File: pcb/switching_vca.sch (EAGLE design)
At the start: 11 parts, among them Q1 MOSFET-PCHANNELSMD, Q2 SST5484, U1 LM319

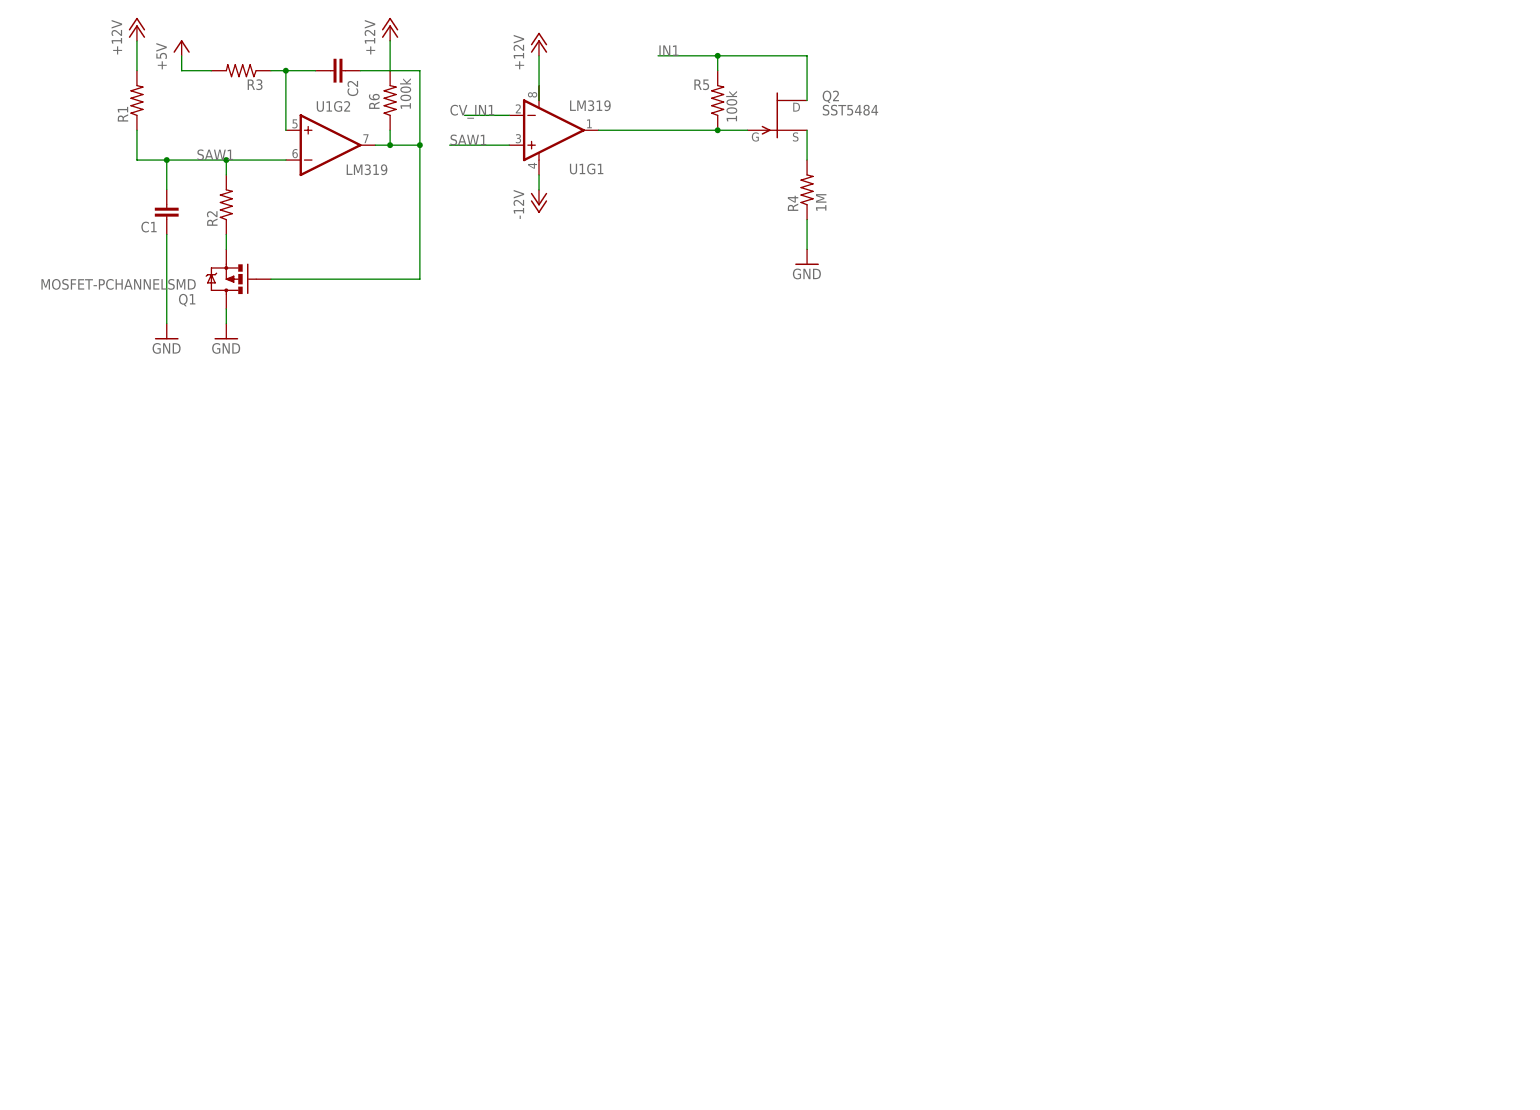
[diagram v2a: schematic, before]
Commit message: First attempt at schem (footprints not specced), initial BOM
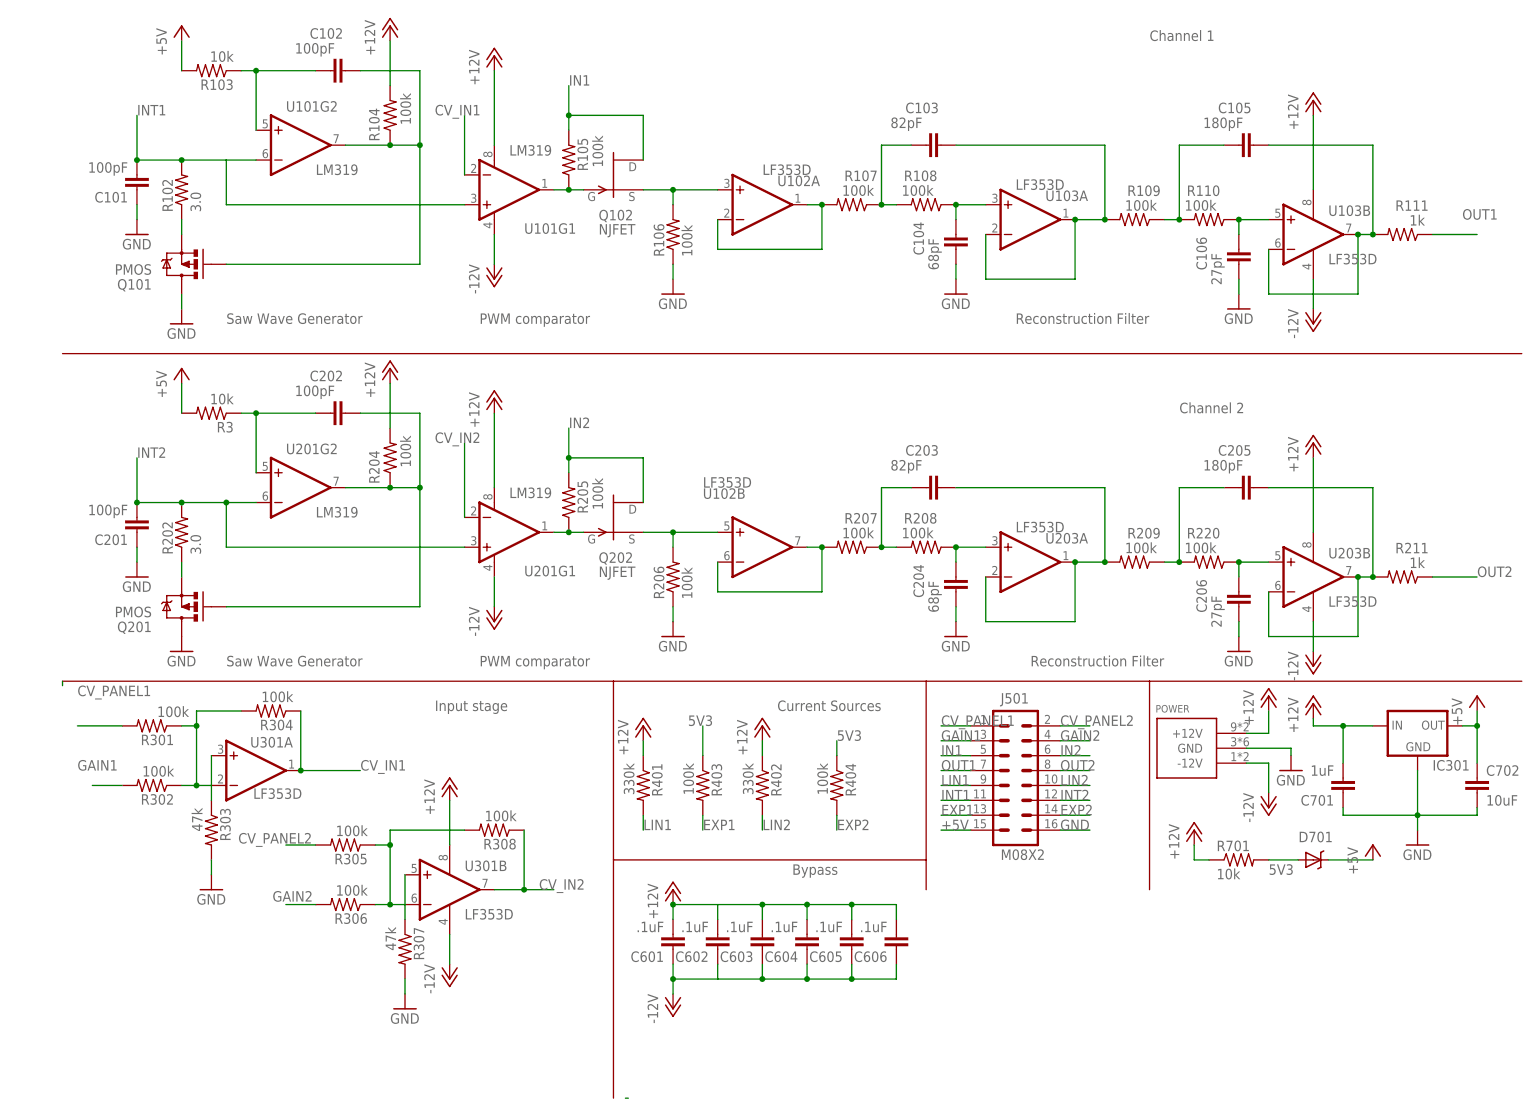
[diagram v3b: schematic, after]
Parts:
- removed C1: (no value), SparkFun:CAP1210
- removed Q1: MOSFET-PCHANNELSMD, SparkFun:MOSFET-PCHANNELSMD
- removed Q2: SST5484, transistor-fet:SST5484
- removed R1, R2: (no value), SparkFun:RESISTOR0603-RES
- removed R4: 1M, SparkFun:RESISTOR0603-RES
- removed R5, R6: 100k, SparkFun:RESISTOR0603-RES
- removed U1: LM319, SparkFun:LM393
- added C101, C201, C202: 100pF, SparkFun:CAP1210
- added C103, C203: 82pF, SparkFun:CAP1210
- added C104, C204: 68pF, SparkFun:CAP1210
- added C105, C205: 180pF, SparkFun:CAP1210
- added C106, C206: 27pF, SparkFun:CAP1210
- added C601, C602, C603, C604, C605, C606: .1uF, SparkFun:CAP1210
- added C701: 1uF, SparkFun:CAP0805
- added C702: 10uF, SparkFun:CAP1206
- added D701: DIODE-SCHOTTKY, SparkFun:DIODE-SCHOTTKY
- added IC301: V_REG_MIC2920, SparkFun:V_REG_MIC2920
- added J501: M08X2, SparkFun:M08X2
- added POWER: POWER_SIMPLE16, eurorack:POWER_SIMPLE16
- added Q101, Q201: PMOS, SparkFun:MOSFET-PCHANNELSMD
- added Q102, Q202: NJFET, transistor-fet:SST5484
- added R102, R202: 3.0, SparkFun:RESISTOR0603-RES
- added R103, R701: 10k, SparkFun:RESISTOR0603-RES
- added R104, R105, R106, R107, R108, R109, R110, R204, R205, R206, R207, R208, R209, R220, R301, R302, R304, R305, R306, R308, R403, R404: 100k, SparkFun:RESISTOR0603-RES
- added R111, R211: 1k, SparkFun:RESISTOR0603-RES
- added R303, R307: 47k, SparkFun:RESISTOR0603-RES
- added R401, R402: 330k, SparkFun:RESISTOR0603-RES
- added U101, U201: LM319, SparkFun:LM393
- added U102, U103, U203, U301: LF353D, linear:LF353D
- C102: value (none) -> 100pF
- R3: value (none) -> 10k
- renumbered C2 to C102
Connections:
- removed net SAW1: C1.2, R1.1, R2.2, U1G1.+IN, U1G2.-IN
- new net -12V: C601.1, C602.1, C603.1, C604.1, C605.1, C606.1, POWER.-12V, U101G1.V-, U103P.V-, U201G1.V-, U203P.V-, U301P.V-
- new net 5V3: D701.A, R403.1, R404.1, R701.2
- new net CV_IN2: R308.1, U201G1.-IN, U301B.OUT
- new net CV_PANEL1: J501.1, R301.2
- new net CV_PANEL2: J501.2, R305.2
- new net EXP1: J501.13, R403.2
- new net EXP2: J501.14, R404.2
- new net GAIN1: J501.3, R302.2
- new net GAIN2: J501.4, R306.2
- new net IN2: J501.6, Q202.D, R205.2
- new net INT1: C101.2, J501.11, R102.2, U101G1.+IN, U101G2.-IN
- new net INT2: C201.2, J501.12, R202.2, U201G1.+IN, U201G2.-IN
- new net LIN1: J501.9, R401.2
- new net LIN2: J501.10, R402.2
- new net N$10: C202.1, Q201.G, R204.1, U201G2.OUT
- new net N$11: C105.2, R109.1, R110.2
- new net N$12: C106.1, R110.1, U103B.+IN
- new net N$13: C105.1, R111.2, U103B.-IN, U103B.OUT
- new net N$15: Q202.G, R205.1, U201G1.OUT
- new net N$16: Q202.S, R206.2, U102B.+IN
- new net N$17: R207.2, U102B.-IN, U102B.OUT
- new net N$18: C203.1, R209.2, U203A.-IN, U203A.OUT
- new net N$19: C203.2, R207.1, R208.2
- new net N$2: R107.2, U102A.-IN, U102A.OUT
- new net N$20: C204.1, R208.1, U203A.+IN
- new net N$21: C205.2, R209.1, R220.2
- new net N$22: C206.1, R220.1, U203B.+IN
- new net N$23: C205.1, R211.2, U203B.-IN, U203B.OUT
- new net N$24: R307.1, U301B.+IN
- new net N$25: R303.1, U301A.+IN
- new net N$32: R305.1, R306.1, R308.2
- new net N$5: C103.1, R109.2, U103A.-IN, U103A.OUT
- new net N$7: C103.2, R107.1, R108.2
- new net N$8: C104.1, R108.1, U103A.+IN
- new net OUT1: J501.7, R111.1
- new net OUT2: J501.8, R211.1
- new net R102: Q201.S, R202.1
- new net R203: C202.2, R3.1, U201G2.+IN
- new net R301: R301.1, R302.1, R304.2, U301A.-IN
- net +12V: now also C601.2, C602.2, C603.2, C604.2, C605.2, C606.2, C701.2, IC301.IN, POWER.+12V, R104.2, R204.2, R401.1, R402.1, R701.1, U101G1.V+, U103P.V+, U201G1.V+, U203P.V+, U301P.V+; no longer R1.2, R6.2
- net +5V: now also C702.1, D701.C, IC301.OUT, J501.15, R103.2
- net CV_IN1: now also R304.1, U101G1.-IN, U301A.OUT; no longer U1G1.-IN
- net GND: now also C101.1, C104.2, C106.2, C201.1, C204.2, C206.2, C701.1, C702.2, IC301.GND, J501.16, POWER.GND, Q101.D, Q201.D, R106.1, R206.1, R303.2, R307.2; no longer C1.1, Q1.D, R4.1
- net IN1: now also J501.5, Q102.D, R105.2; no longer Q2.D, R5.2
- net N$: now also Q101.G, R104.1, U101G2.OUT; no longer Q1.G, R6.1, U1G2.OUT
- net N$1: now also Q101.S, R102.1; no longer Q1.S, R2.1
- net N$3: now also Q102.G, R105.1, U101G1.OUT; no longer Q2.G, R5.1, U1G1.OUT
- net N$4: now also R103.1, U101G2.+IN; no longer R3.1, U1G2.+IN
- net N$6: now also Q102.S, R106.2, U102A.+IN; no longer Q2.S, R4.2
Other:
- note added: "Bypass"
- note added: "Channel 1"
- note added: "Channel 2"
- note added: "Current Sources"
- note added: "Input stage"
- note added: "PWM comparator"
- note added: "Reconstruction Filter"
- note added: "Saw Wave Generator"
- moved on the sheet: R3

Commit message: added shitty board, made mouser bom
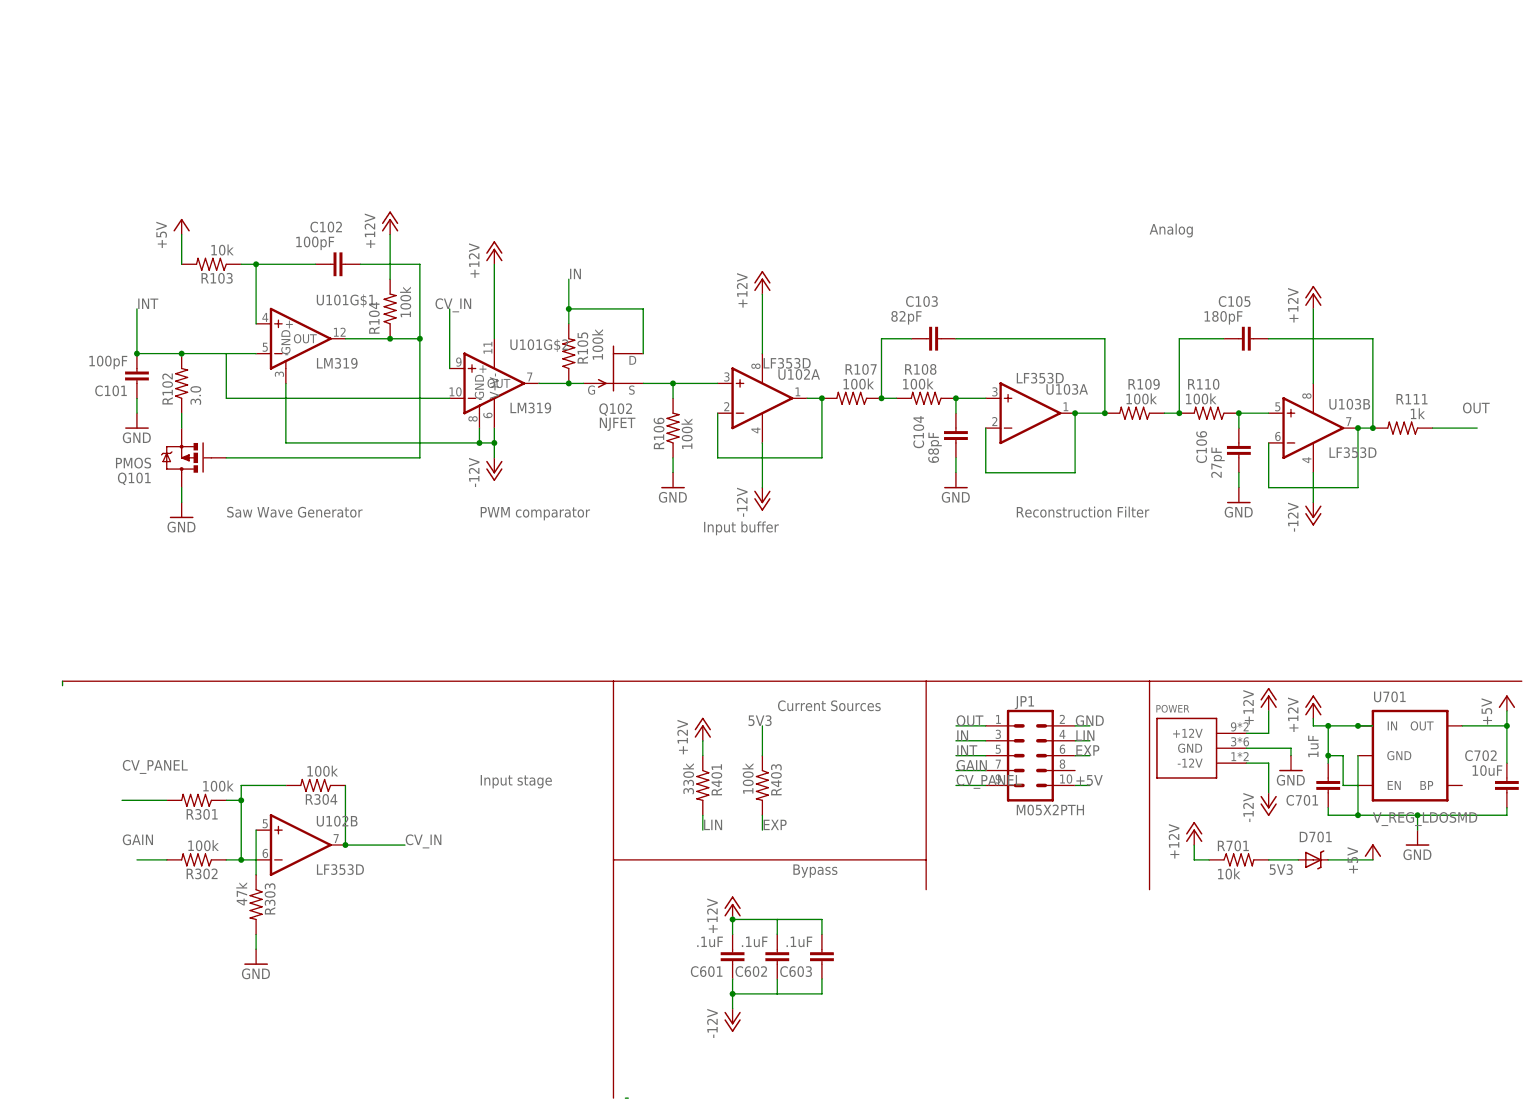
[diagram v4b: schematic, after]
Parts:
- removed C201, C202: 100pF, SparkFun:CAP1210
- removed C203: 82pF, SparkFun:CAP1210
- removed C204: 68pF, SparkFun:CAP1210
- removed C205: 180pF, SparkFun:CAP1210
- removed C206: 27pF, SparkFun:CAP1210
- removed C604, C605, C606: .1uF, SparkFun:CAP1210
- removed IC301: V_REG_MIC2920, SparkFun:V_REG_MIC2920
- removed J501: M08X2, SparkFun:M08X2
- removed Q201: PMOS, SparkFun:MOSFET-PCHANNELSMD
- removed Q202: NJFET, transistor-fet:SST5484
- removed R202: 3.0, SparkFun:RESISTOR0603-RES
- removed R204, R205, R206, R207, R208, R209, R220, R305, R306, R308, R404: 100k, SparkFun:RESISTOR0603-RES
- removed R211: 1k, SparkFun:RESISTOR0603-RES
- removed R3: 10k, SparkFun:RESISTOR0603-RES
- removed R307: 47k, SparkFun:RESISTOR0603-RES
- removed R402: 330k, SparkFun:RESISTOR0603-RES
- removed U201: LM319, SparkFun:LM393
- removed U203, U301: LF353D, linear:LF353D
- added JP1: M05X2PTH, SparkFun:M05X2PTH
- added U701: V_REG_LDOSMD, SparkFun:V_REG_LDOSMD
- C101, C102, C103, C104, C105, C106, C601, C602, C603: device SparkFun:CAP1210 -> SparkFun:CAP0603-CAP
- U101: device SparkFun:LM393 -> russruss:LM319
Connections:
- removed net CV_IN1: R304.1, U101G1.-IN, U301A.OUT
- removed net CV_IN2: R308.1, U201G1.-IN, U301B.OUT
- removed net CV_PANEL1: J501.1, R301.2
- removed net CV_PANEL2: J501.2, R305.2
- removed net EXP1: J501.13, R403.2
- removed net EXP2: J501.14, R404.2
- removed net GAIN1: J501.3, R302.2
- removed net GAIN2: J501.4, R306.2
- removed net IN1: J501.5, Q102.D, R105.2
- removed net IN2: J501.6, Q202.D, R205.2
- removed net INT1: C101.2, J501.11, R102.2, U101G1.+IN, U101G2.-IN
- removed net INT2: C201.2, J501.12, R202.2, U201G1.+IN, U201G2.-IN
- removed net LIN1: J501.9, R401.2
- removed net LIN2: J501.10, R402.2
- removed net N$15 (its old number): Q202.G, R205.1, U201G1.OUT
- removed net N$16: Q202.S, R206.2, U102B.+IN
- removed net N$17: R207.2, U102B.-IN, U102B.OUT
- removed net N$18: C203.1, R209.2, U203A.-IN, U203A.OUT
- removed net N$19: C203.2, R207.1, R208.2
- removed net N$20: C204.1, R208.1, U203A.+IN
- removed net N$21: C205.2, R209.1, R220.2
- removed net N$22: C206.1, R220.1, U203B.+IN
- removed net N$23: C205.1, R211.2, U203B.-IN, U203B.OUT
- removed net N$24: R307.1, U301B.+IN
- removed net N$25: R303.1, U301A.+IN
- removed net N$32: R305.1, R306.1, R308.2
- removed net OUT1: J501.7, R111.1
- removed net OUT2: J501.8, R211.1
- removed net R102: Q201.S, R202.1
- removed net R203: C202.2, R3.1, U201G2.+IN
- new net CV_IN: R304.1, U102B.OUT
- new net CV_PANEL: JP1.9, R301.2
- new net EXP: JP1.6, R403.2
- new net GAIN: JP1.7, R302.2
- new net IN: JP1.3, Q102.D, R105.2
- new net INT: C101.2, JP1.5, R102.2, U101G$1.-, U101G$2.-
- new net LIN: JP1.4, R401.2
- new net OUT: JP1.1, R111.1
- net +12V: now also U101G$3.V+, U102P.V+, U701.EN, U701.IN; no longer C604.2, C605.2, C606.2, IC301.IN, R204.2, R402.1, U101G1.V+, U201G1.V+, U203P.V+, U301P.V+
- net +5V: now also JP1.10, U701.OUT; no longer IC301.OUT, J501.15, R3.2
- net -12V: now also U101G$1.GND, U101G$2.GND, U101G$3.V-, U102P.V-; no longer C604.1, C605.1, C606.1, U101G1.V-, U201G1.V-, U203P.V-, U301P.V-
- net 5V3: no longer R404.1
- net GND: now also JP1.2, U701.GND; no longer C201.1, C204.2, C206.2, IC301.GND, J501.16, Q201.D, R206.1, R307.2
- net N$: now also U101G$1.OUT; no longer U101G2.OUT
- net N$10: now also R303.1, U102B.+IN; no longer C202.1, Q201.G, R204.1, U201G2.OUT
- net N$3: now also U101G$2.OUT; no longer U101G1.OUT
- net N$4: now also U101G$1.+; no longer U101G2.+IN
- net R301: now also U102B.-IN; no longer U301A.-IN
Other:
- note added: "Analog"
- note added: "Input buffer"
- note removed: "Channel 1"
- note removed: "Channel 2"
- moved on the sheet: C101, C102, C103, C104, C105, C106, C601, C602, C603, C701, C702, Q101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

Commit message: Routed the board with a travesty of VIAs
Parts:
- added TP101: M01PTH, SparkFun:M01PTH
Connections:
- net IN: now also JP1.8; no longer JP1.3
- net N$15: now also TP101.1
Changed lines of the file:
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@@
 <setting verticaltext="up"/>
 </settings>
-<grid distance="0.1" unitdist="inch" unit="inch" style="lines" multiple="1" display="no" altdistance="0.01" altunitdist="inch" altunit="inch"/>
+<grid distance="0.1" unitdist="inch" unit="inch" style="lines" multiple="1" display="yes" altdistance="0.01" altunitdist="inch" altunit="inch"/>
 <layers>
 <layer number="1" name="Top" color="4" fill="1" visible="no" active="no"/>
@@
 <part name="U701" library="SparkFun" deviceset="V_REG_LDO" device="SMD"/>
 <part name="U101" library="russruss" deviceset="LM319" device=""/>
+<part name="TP101" library="SparkFun" deviceset="M01" device="PTH" value=""/>
 </parts>
 <sheets>
@@
 <instance part="U101" gate="G$2" x="73.66" y="121.92"/>
 <instance part="U101" gate="G$3" x="73.66" y="121.92"/>
+<instance part="TP101" gate="G$1" x="129.54" y="101.6" rot="R90"/>
 </instances>
 <busses>
@@
 </segment>
 <segment>
-<pinref part="JP1" gate="G$1" pin="3"/>
-<wire x1="157.48" y1="60.96" x2="152.4" y2="60.96" width="0.1524" layer="91"/>
-<label x="152.4" y="60.96" size="1.778" layer="95"/>
+<pinref part="JP1" gate="G$1" pin="8"/>
+<wire x1="172.72" y1="55.88" x2="175.26" y2="55.88" width="0.1524" layer="91"/>
+<label x="172.72" y="55.88" size="1.778" layer="95"/>
 </segment>
 </net>
@@
 <wire x1="111.76" y1="116.84" x2="111.76" y2="109.22" width="0.1524" layer="91"/>
 <wire x1="111.76" y1="109.22" x2="129.54" y2="109.22" width="0.1524" layer="91"/>
-</segment>
-</net>
+<pinref part="TP101" gate="G$1" pin="1"/>
+<junction x="129.54" y="109.22"/>
+</segment>
+</net>
